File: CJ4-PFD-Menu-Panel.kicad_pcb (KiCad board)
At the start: 2 copper layers, 122 x 57 mm, 54 parts, among them J1 Conn_01x02, J2 Conn_01x02, J3 Conn_01x02, J4 USB_B_Micro, J5 RP2040_SWD, J6 TC2030-IDC-NL, SW1 SW_PUSH_LED, SW10 SW_PUSH_LED, SW11 SW_PUSH_LED, SW2 SW_PUSH_LED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

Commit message: Final changes prior to ordering
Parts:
- R1: value R_Small -> 3k; footprint Custom_Footprints:Perfect_0402 -> Resistor_SMD:R_0805_2012Metric_Pad1.20x1.40mm_HandSolder
- U2: value XC6206P332MR -> AMS1117-3.3; footprint Package_TO_SOT_SMD:SOT-23 -> Package_TO_SOT_SMD:SOT-223-3_TabPin2
- moved R6 25.4 mm to (123.6, 67.2)
- moved R7 25.4 mm to (123.6, 65.2)
- moved C9 7.85 mm to (86.0, 54.9)
- moved U2 6.01 mm to (91.2, 54.9), turned to 180 degrees
- moved C7 4.56 mm to (96.3, 56.6)
- moved R1 0.98 mm to (50.0, 60.6)
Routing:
- net /RP2040/USB_D+: track 35.7 -> 7.45 mm, vias 1 -> 0
- net /RP2040/USB_D-: track 30.8 -> 4.85 mm, vias 1 -> 0
- net /RP2040/USB_D_R-: track 25.7 -> 51.5 mm
- net /RP2040/USB_D_R+: track 26.2 -> 51.7 mm
- net +3V3: track 277.6 -> 270.6 mm, vias 11 -> 10
- net +5V: track 147.1 -> 144.5 mm, vias 1 -> 2
- net /TFC: track 108.4 -> 105.9 mm
- net /LED_TFC: track 119.2 -> 116.7 mm
- net GND: track 29.6 -> 31.1 mm
- added copper zone on B.Cu, net +3V3

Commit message: Update part rotation
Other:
- board text added: "*"
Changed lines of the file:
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@@
     (effects (font (size 1.5 1.5) (thickness 0.3)))
+  )
+  (gr_text "*" (at 85.725 69.088 -180) (layer "B.SilkS")
+    (effects (font (size 1 1) (thickness 0.15)) (justify mirror))
   )
   (gr_text "SWD" (at 60.96 51.689) (layer "B.SilkS")
@@
     (effects (font (size 1 1) (thickness 0.15)) (justify mirror))
   )
+  (gr_text "*" (at 50.8 69.85 -180) (layer "B.SilkS")
+    (effects (font (size 1 1) (thickness 0.15)) (justify mirror))
+  )
   (gr_text "GND" (at 71.12 51.689) (layer "B.SilkS")
     (effects (font (size 1 1) (thickness 0.15)) (justify mirror))
   )
   (gr_text "MASTER WARNING" (at 29.337 41.529 270) (layer "B.SilkS")
+    (effects (font (size 1 1) (thickness 0.15)) (justify mirror))
+  )
+  (gr_text "*" (at 94.361 50.292 -180) (layer "B.SilkS")
     (effects (font (size 1 1) (thickness 0.15)) (justify mirror))
   )
@@
     (effects (font (size 1 1) (thickness 0.15)) (justify mirror))
   )
+  (gr_text "*" (at 61.849 62.484 -180) (layer "B.SilkS")
+    (effects (font (size 1 1) (thickness 0.15)) (justify mirror))
+  )

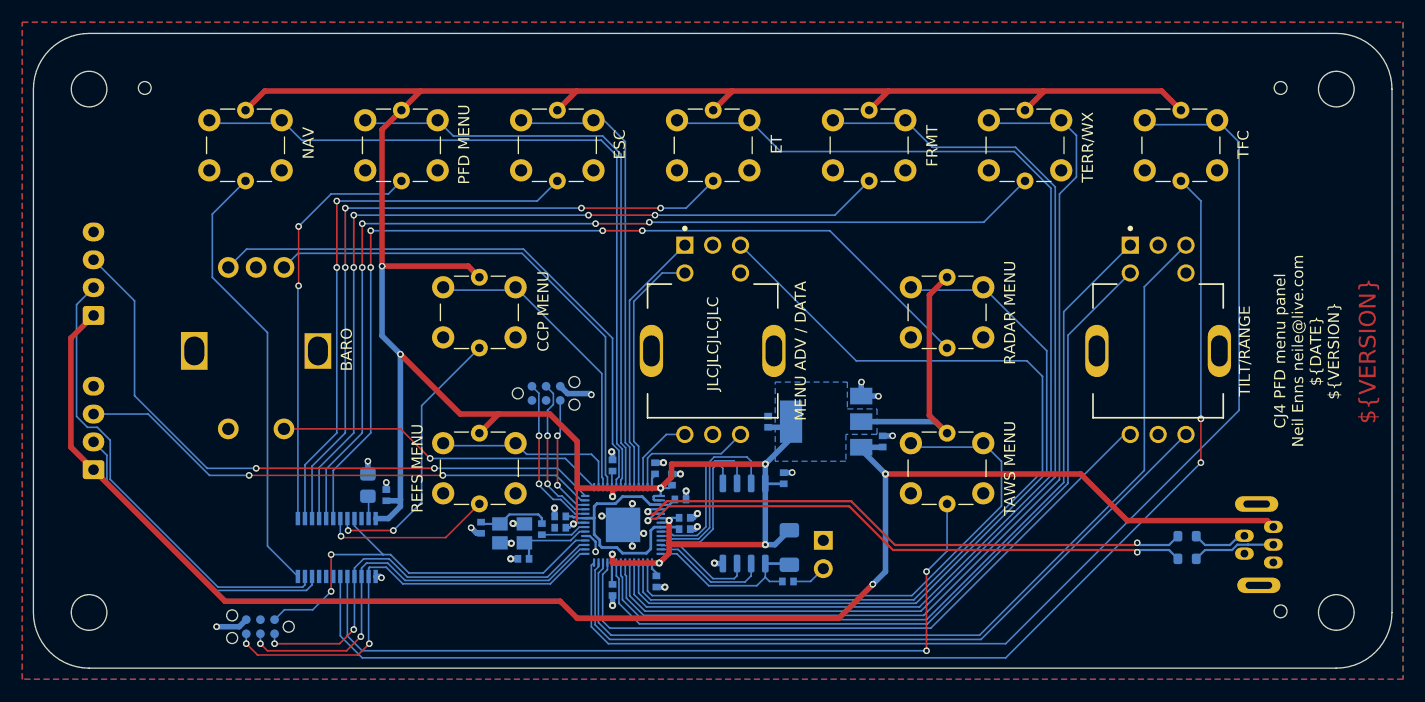
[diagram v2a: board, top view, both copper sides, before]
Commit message: Fix copper fill, add via stitching
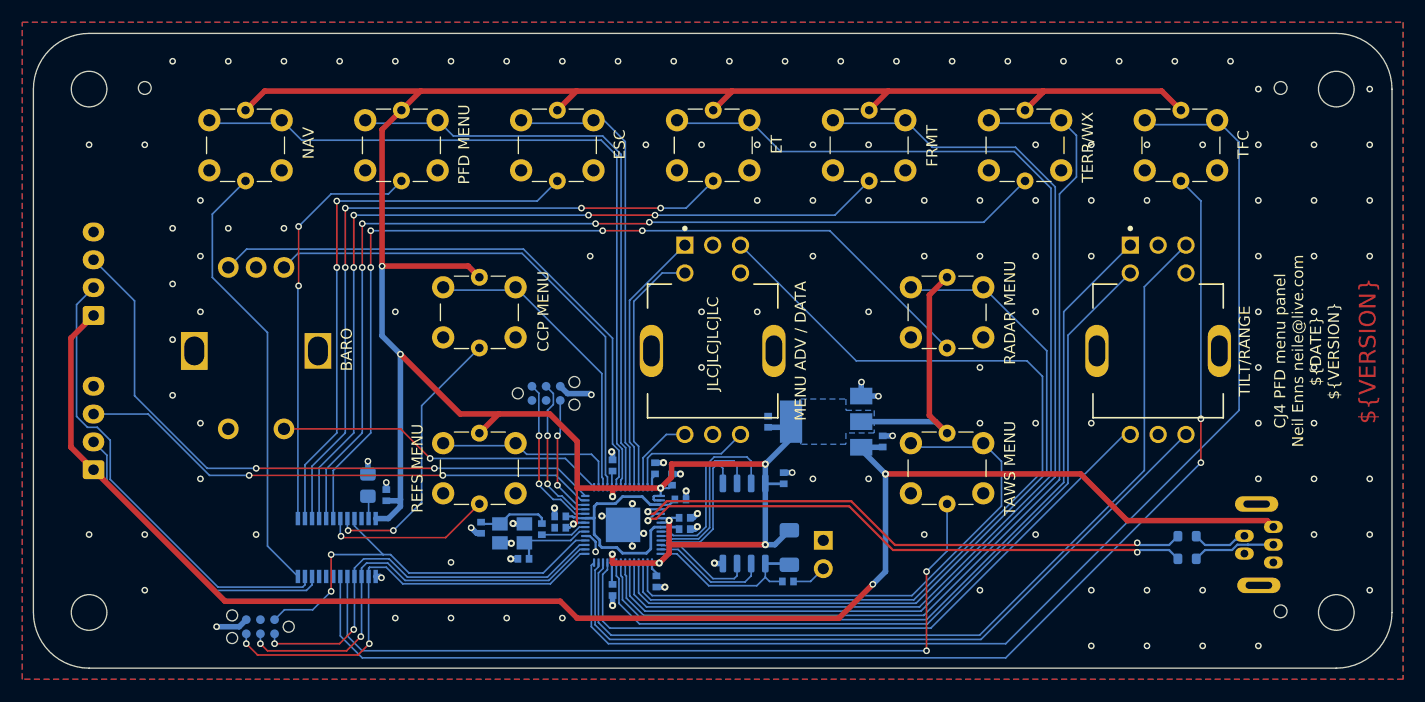
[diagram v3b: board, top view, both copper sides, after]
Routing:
- net GND: vias 28 -> 138
